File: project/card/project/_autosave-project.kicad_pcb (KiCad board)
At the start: 2 copper layers, 34 parts, among them J1 USB_OTG, J2 Conn_01x06_Male, J3 Conn_01x02_Male, J5 Conn_Coaxial, J6 Conn_01x07_Female, J7 Conn_01x05_Female, SW1 SW_Push, SW2 SW_Push, U1 LM1117ADJ, U2 CMWX1ZZABZ-078

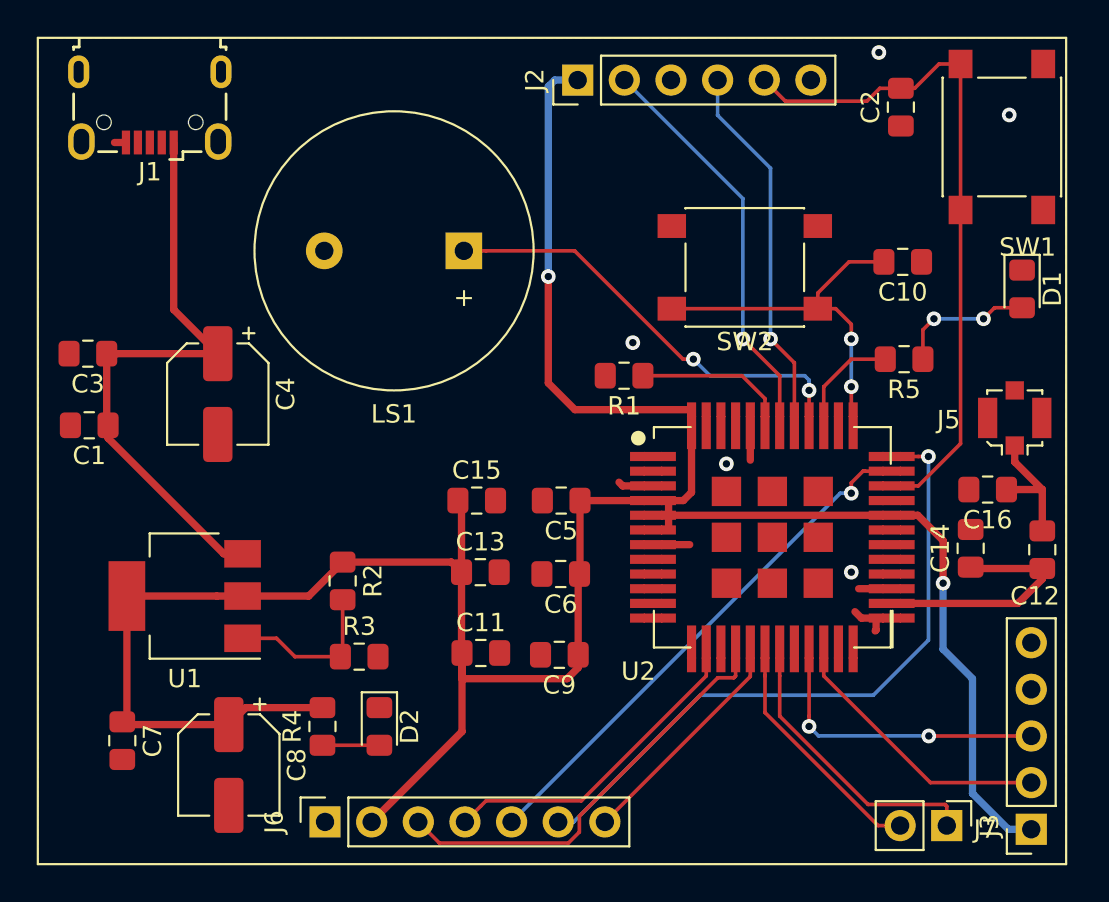
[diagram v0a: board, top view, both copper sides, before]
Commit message: fix routes and generate gerber
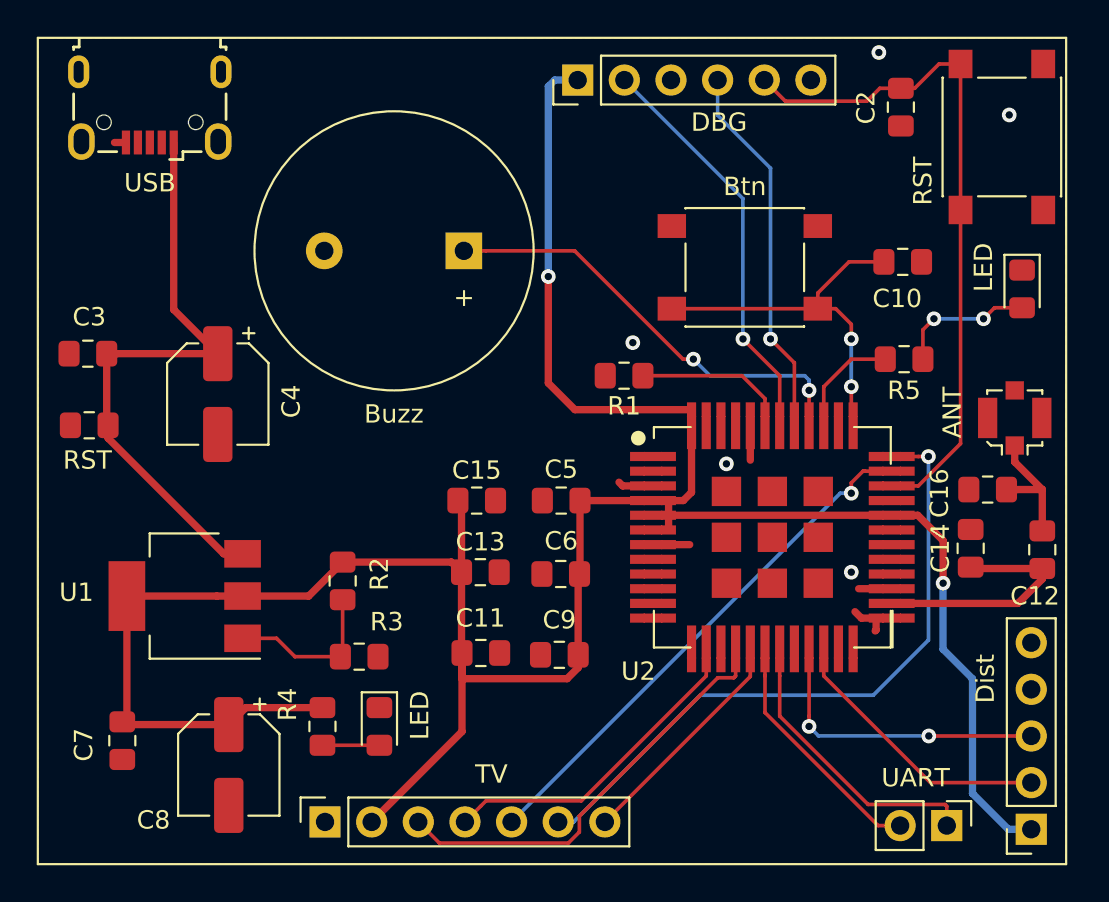
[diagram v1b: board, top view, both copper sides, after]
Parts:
- renumbered J5 to ANT, SW2 to Btn, LS1 to Buzz, J2 to DBG, J7 to Dist, D2 to LED, D1 to LED, SW1 to RST, C1 to RST, J6 to TV, J3 to UART, J1 to USB
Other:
- net class Power: trace_width 0.4 -> 0.5
